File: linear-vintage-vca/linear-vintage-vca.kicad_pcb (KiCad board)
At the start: 2 copper layers, 50.5 x 110 mm, 57 parts, among them J1 Conn_02x08_Odd_Even, J10 Conn_01x02_Pin, J11 Conn_01x02_Pin, J2 AudioJack2, J3 AudioJack2, J4 AudioJack2, J5 AudioJack2, J6 AudioJack2, J7 AudioJack2, J8 AudioJack2, J9 AudioJack2, Q1 BC556, Q2 BC556, SW1 SW_SPDT_321, SW2 SW_SPDT_321, U1 LM13700, U2 TL072, U3 TL072

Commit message: Version sent to jlcpcb
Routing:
- net Net-(J11-Pin_2): track 50.0 -> 53.9 mm
- net Net-(J11-Pin_1): track 18.1 -> 19.2 mm
- net Net-(R4-Pad2): track 40.9 -> 41.8 mm
- net Net-(SW2-C): track 19.2 -> 20.0 mm
- net Net-(U3A--): track 58.8 -> 59.6 mm
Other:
- board text added: "2025"
- board text added: "Linear VCA"
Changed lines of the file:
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@@
 			(outputformat 1)
 			(mirror no)
-			(drillshape 1)
+			(drillshape 0)
 			(scaleselection 1)
-			(outputdirectory "")
+			(outputdirectory "gerber")
 		)
 	)
@@
 		(tags "Resistor Axial_DIN0207 series Axial Horizontal pin pitch 7.62mm 0.25W = 1/4W length 6.3mm diameter 2.5mm")
 		(property "Reference" "R21"
-			(at -2.38 0.2 90)
+			(at 10.42 0 180)
 			(layer "F.SilkS")
 			(effects
@@
 		(tags "Resistor Axial_DIN0207 series Axial Horizontal pin pitch 7.62mm 0.25W = 1/4W length 6.3mm diameter 2.5mm")
 		(property "Reference" "R22"
-			(at 10.01 0 90)
+			(at -2.79 -0.8 180)
 			(layer "F.SilkS")
 			(effects
@@
 		(tags "C Rect series Radial pin pitch 5.00mm length 7mm width 2mm Capacitor")
 		(property "Reference" "C5"
-			(at 7.533333 0 0)
+			(at 5.133333 2 0)
 			(layer "F.SilkS")
 			(effects
@@
 		(tags "TRS audio jack stereo horizontal")
 		(property "Reference" "J8"
-			(at 0 -6 90)
+			(at 5.605 5 180)
 			(layer "F.SilkS")
 			(effects
@@
 	)
 	(gr_text "Output"
-		(at 100.4 165.4 90)
+		(at 100.2 165.4 90)
 		(layer "F.SilkS")
 		(effects
@@
 		)
 	)
+	(gr_text "Linear VCA"
+		(at 96 118.8 0)
+		(layer "B.SilkS")
+		(effects
+			(font
+				(size 5 5)
+				(thickness 0.7)
+			)
+			(justify left bottom mirror)
+		)
+	)
+	(gr_text "2025"
+		(at 72 123.4 0)
+		(layer "B.SilkS")
+		(effects
+			(font
+				(size 3 3)
+				(thickness 0.3)
+			)
+			(justify left bottom mirror)
+		)
+	)
 	(dimension
 		(type orthogonal)
@@
 	)
 	(segment
-		(start 77.2 154.533333)
-		(end 77.2 143.061667)
+		(start 78.666667 156)
+		(end 76.2 153.533333)
 		(width 0.4)
 		(layer "B.Cu")
@@
 	)
 	(segment
-		(start 77.2 143.061667)
-		(end 81.166667 139.095)
+		(start 76.2 153.533333)
+		(end 76.2 144.061667)
 		(width 0.4)
 		(layer "B.Cu")
@@
 	)
 	(segment
-		(start 78.666667 156)
-		(end 77.2 154.533333)
+		(start 76.2 144.061667)
+		(end 81.166667 139.095)
 		(width 0.4)
 		(layer "B.Cu")
@@
 	)
 	(segment
-		(start 74.512083 134.487917)
-		(end 74.6 134.4)
+		(start 75.6 165)
+		(end 75.6 135.4)
 		(width 0.4)
 		(layer "B.Cu")
@@
 	)
 	(segment
-		(start 73.143333 134.487917)
-		(end 74.512083 134.487917)
+		(start 73.143333 167.2)
+		(end 73.143333 167.343333)
 		(width 0.4)
 		(layer "B.Cu")
@@
 	)
 	(segment
-		(start 73.2 167.4)
-		(end 74.6 166)
+		(start 74.512083 134.487917)
+		(end 74.6 134.4)
 		(width 0.4)
 		(layer "B.Cu")
@@
 	)
 	(segment
-		(start 73.186967 129.386967)
-		(end 73.143333 129.386967)
+		(start 73.143333 134.487917)
+		(end 74.512083 134.487917)
 		(width 0.4)
 		(layer "B.Cu")
@@
 	)
 	(segment
-		(start 74.6 130.8)
-		(end 73.186967 129.386967)
+		(start 75.6 135.4)
+		(end 74.6 134.4)
 		(width 0.4)
 		(layer "B.Cu")
@@
 	)
 	(segment
-		(start 73.143333 167.2)
-		(end 73.143333 167.343333)
+		(start 73.186967 129.386967)
+		(end 73.143333 129.386967)
 		(width 0.4)
 		(layer "B.Cu")
@@
 	)
 	(segment
-		(start 74.6 134.4)
-		(end 74.6 130.8)
+		(start 74.6 130.8)
+		(end 73.186967 129.386967)
 		(width 0.4)
 		(layer "B.Cu")
@@
 	)
 	(segment
-		(start 74.6 166)
-		(end 74.6 134.4)
+		(start 73.2 167.4)
+		(end 75.6 165)
+		(width 0.4)
+		(layer "B.Cu")
+		(net 32)
+	)
+	(segment
+		(start 74.6 134.4)
+		(end 74.6 130.8)
 		(width 0.4)
 		(layer "B.Cu")
@@
 	)
 	(segment
-		(start 87 130.023333)
+		(start 86.6 129.623333)
 		(end 84.976667 128)
 		(width 0.4)
@@
 	)
 	(segment
-		(start 89.2 151.6)
-		(end 87 149.4)
+		(start 89.19 151.61)
+		(end 89.2 151.6)
 		(width 0.4)
 		(layer "B.Cu")
@@
 	)
 	(segment
-		(start 89.19 151.61)
-		(end 89.2 151.6)
+		(start 86.6 149)
+		(end 86.6 129.623333)
 		(width 0.4)
 		(layer "B.Cu")
@@
 	)
 	(segment
-		(start 87 149.4)
-		(end 87 130.023333)
+		(start 89.2 151.6)
+		(end 86.6 149)
 		(width 0.4)
 		(layer "B.Cu")
@@
 	)
 	(segment
-		(start 96.678578 146.91347)
-		(end 96.82 146.91347)
+		(start 75.4 107.260533)
+		(end 73.143333 105.003866)
 		(width 0.4)
 		(layer "B.Cu")
@@
 	)
 	(segment
-		(start 75.4 107.260533)
-		(end 73.143333 105.003866)
+		(start 75.4 117.8)
+		(end 75.4 107.260533)
 		(width 0.4)
 		(layer "B.Cu")
@@
 	)
 	(segment
-		(start 75.4 117.8)
-		(end 75.4 107.260533)
+		(start 86.46 125.46)
+		(end 93 132)
 		(width 0.4)
 		(layer "B.Cu")
@@
 	)
 	(segment
-		(start 96.82 146.91347)
+		(start 96.82 147.62)
 		(end 96.82 151.6)
 		(width 0.4)
@@
 	(segment
 		(start 84.976667 125.46)
-		(end 87.601 128.084333)
+		(end 86.46 125.46)
 		(width 0.4)
 		(layer "B.Cu")
@@
 	)
 	(segment
-		(start 87.601 128.084333)
-		(end 87.601 137.835892)
+		(start 93 132)
+		(end 93 143.8)
 		(width 0.4)
 		(layer "B.Cu")
@@
 	)
 	(segment
-		(start 87.601 137.835892)
-		(end 96.678578 146.91347)
+		(start 93 143.8)
+		(end 96.82 147.62)
 		(width 0.4)
 		(layer "B.Cu")
@@
 	)
 	(segment
-		(start 83.666667 153.835)
-		(end 82.431667 152.6)
+		(start 84.4 155.266667)
+		(end 84.4 152.6)
 		(width 0.4)
 		(layer "B.Cu")
@@
 	)
 	(segment
-		(start 82.6 119)
-		(end 85.2 116.4)
+		(start 82.431667 152.6)
+		(end 84.4 152.6)
 		(width 0.4)
 		(layer "B.Cu")
@@
 	)
 	(segment
-		(start 85.2 109.823333)
-		(end 84.976667 109.6)
+		(start 84.4 137)
+		(end 82.6 135.2)
 		(width 0.4)
 		(layer "B.Cu")
@@
 	)
 	(segment
-		(start 85.2 116.4)
-		(end 85.2 109.823333)
+		(start 84.4 148.4)
+		(end 84.4 137)
 		(width 0.4)
 		(layer "B.Cu")
@@
 	)
 	(segment
-		(start 82.6 137.214932)
-		(end 82.6 119)
+		(start 85.2 109.823333)
+		(end 84.976667 109.6)
 		(width 0.4)
 		(layer "B.Cu")
@@
 	)
 	(segment
-		(start 83.6 138.214932)
-		(end 82.6 137.214932)
+		(start 82.6 119)
+		(end 85.2 116.4)
 		(width 0.4)
 		(layer "B.Cu")
@@
 	)
 	(segment
-		(start 81.166667 148.495)
-		(end 83.6 146.061667)
+		(start 82.6 135.2)
+		(end 82.6 119)
 		(width 0.4)
 		(layer "B.Cu")
@@
 	)
 	(segment
-		(start 82.431667 149.831667)
-		(end 82.431667 152.6)
+		(start 84.305 148.495)
+		(end 84.4 148.4)
 		(width 0.4)
 		(layer "B.Cu")
@@
 	)
 	(segment
-		(start 83.666667 156)
-		(end 83.666667 153.835)
+		(start 85.2 116.4)
+		(end 85.2 109.823333)
+		(width 0.4)
+		(layer "B.Cu")
+		(net 44)
+	)
+	(segment
+		(start 81.166667 148.495)
+		(end 84.305 148.495)
 		(width 0.4)
 		(layer "B.Cu")
@@
 	)
 	(segment
-		(start 83.6 146.061667)
-		(end 83.6 138.214932)
+		(start 83.666667 156)
+		(end 84.4 155.266667)
 		(width 0.4)
 		(layer "B.Cu")
@@
 	)
 	(segment
-		(start 81.166667 148.566667)
-		(end 82.431667 149.831667)
+		(start 84.4 152.6)
+		(end 84.4 148.4)
 		(width 0.4)
 		(layer "B.Cu")
@@
 	)
 	(segment
+		(start 77.6 150.308333)
+		(end 77.6 146.2)
+		(width 0.4)
+		(layer "F.Cu")
+		(net 46)
+	)
+	(segment
 		(start 88.5 143.795)
 		(end 81.166667 143.795)
@@
 	)
 	(segment
-		(start 79.891667 152.6)
-		(end 78.2 150.908333)
+		(start 77.6 146.2)
+		(end 80.005 143.795)
 		(width 0.4)
-		(layer "B.Cu")
+		(layer "F.Cu")
 		(net 46)
 	)
 	(segment
-		(start 78.2 146.761667)
+		(start 80.005 143.795)
 		(end 81.166667 143.795)
 		(width 0.4)
-		(layer "B.Cu")
+		(layer "F.Cu")
 		(net 46)
 	)
 	(segment
-		(start 78.2 150.908333)
-		(end 78.2 146.761667)
+		(start 79.891667 152.6)
+		(end 77.6 150.308333)
 		(width 0.4)
-		(layer "B.Cu")
+		(layer "F.Cu")
 		(net 46)
 	)

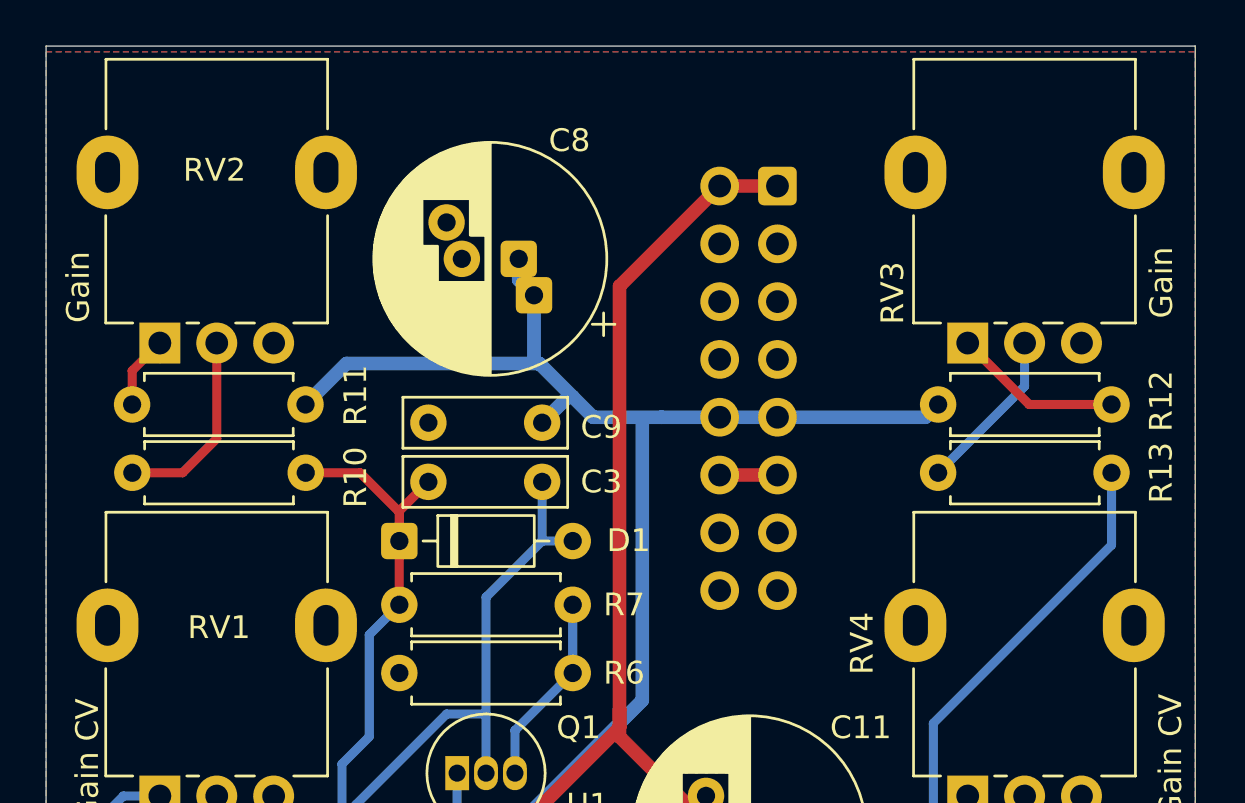
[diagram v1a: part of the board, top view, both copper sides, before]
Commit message: Fix potentiometers footprint.
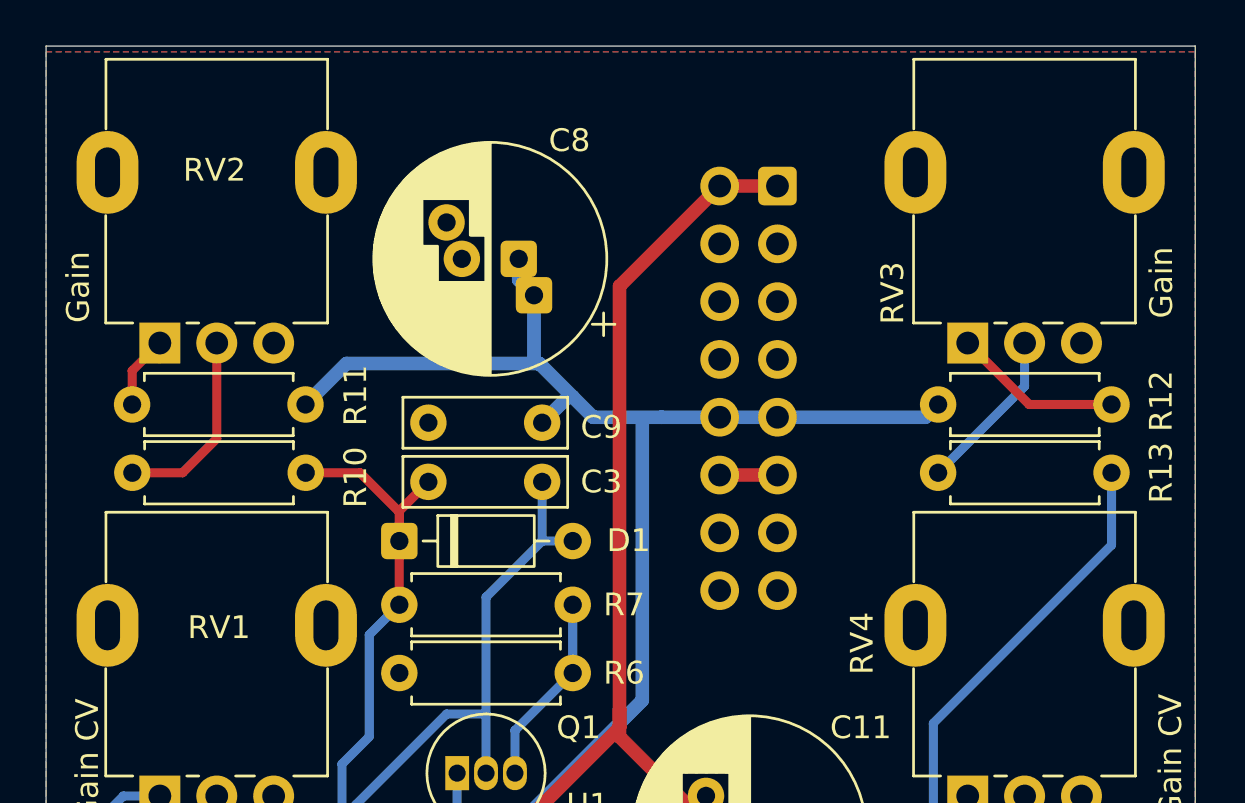
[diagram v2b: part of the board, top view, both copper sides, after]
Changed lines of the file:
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@@
 		(pad "" thru_hole oval
 			(at -4.8 0 180)
-			(size 2.72 3.24)
-			(drill oval 1.1 1.8)
+			(size 2.72 3.64)
+			(drill oval 1.1 2.2)
 			(layers "*.Cu" "*.Mask")
 			(remove_unused_layers no)
@@
 		(pad "" thru_hole oval
 			(at 4.8 0 180)
-			(size 2.72 3.24)
-			(drill oval 1.1 1.8)
+			(size 2.72 3.64)
+			(drill oval 1.1 2.2)
 			(layers "*.Cu" "*.Mask")
 			(remove_unused_layers no)
@@
 		(pad "" thru_hole oval
 			(at -4.8 0 180)
-			(size 2.72 3.24)
-			(drill oval 1.1 1.8)
+			(size 2.72 3.64)
+			(drill oval 1.1 2.2)
 			(layers "*.Cu" "*.Mask")
 			(remove_unused_layers no)
@@
 		(pad "" thru_hole oval
 			(at 4.8 0 180)
-			(size 2.72 3.24)
-			(drill oval 1.1 1.8)
+			(size 2.72 3.64)
+			(drill oval 1.1 2.2)
 			(layers "*.Cu" "*.Mask")
 			(remove_unused_layers no)
@@
 		(pad "" thru_hole oval
 			(at -4.8 0 180)
-			(size 2.72 3.24)
-			(drill oval 1.1 1.8)
+			(size 2.72 3.64)
+			(drill oval 1.1 2.2)
 			(layers "*.Cu" "*.Mask")
 			(remove_unused_layers no)
@@
 		(pad "" thru_hole oval
 			(at 4.8 0 180)
-			(size 2.72 3.24)
-			(drill oval 1.1 1.8)
+			(size 2.72 3.64)
+			(drill oval 1.1 2.2)
 			(layers "*.Cu" "*.Mask")
 			(remove_unused_layers no)
@@
 		(pad "" thru_hole oval
 			(at -4.8 0 180)
-			(size 2.72 3.24)
-			(drill oval 1.1 1.8)
+			(size 2.72 3.64)
+			(drill oval 1.1 2.2)
 			(layers "*.Cu" "*.Mask")
 			(remove_unused_layers no)
@@
 		(pad "" thru_hole oval
 			(at 4.8 0 180)
-			(size 2.72 3.24)
-			(drill oval 1.1 1.8)
+			(size 2.72 3.64)
+			(drill oval 1.1 2.2)
 			(layers "*.Cu" "*.Mask")
 			(remove_unused_layers no)

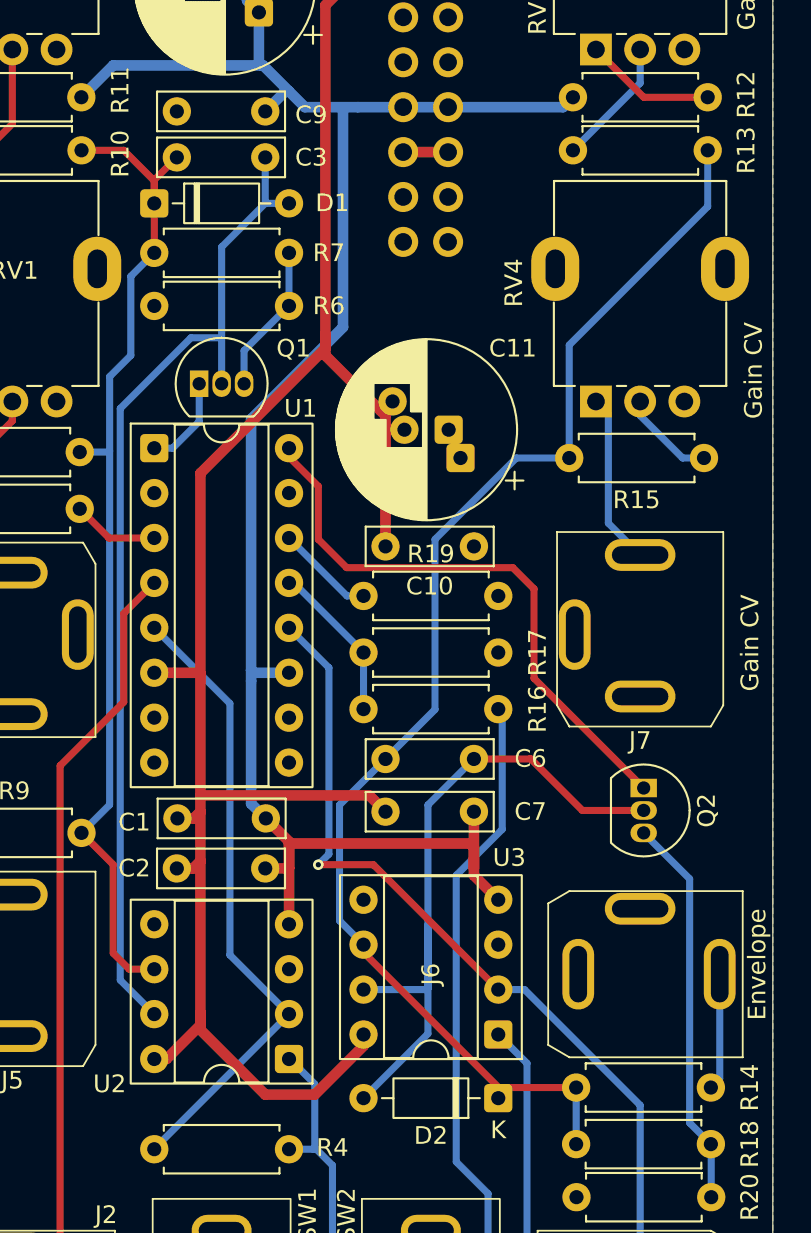
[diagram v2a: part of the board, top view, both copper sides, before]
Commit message: Cleaned up footprints
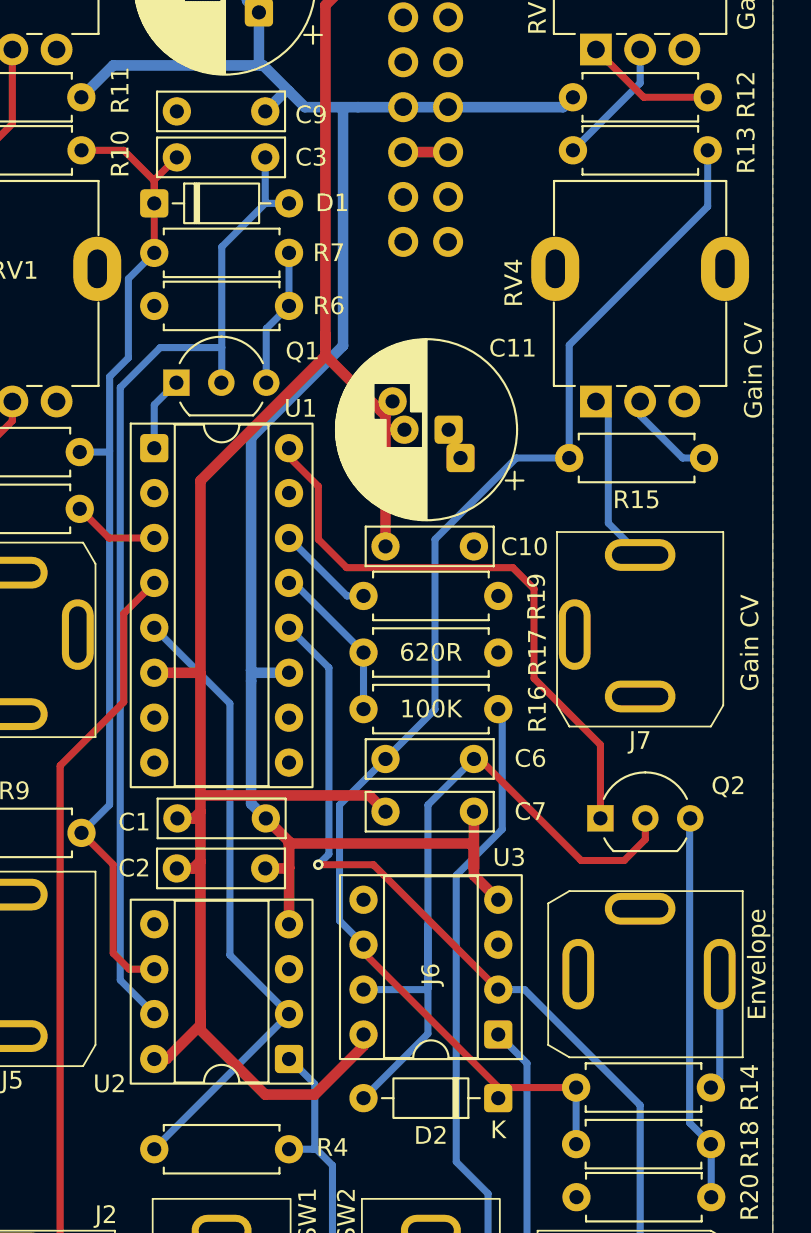
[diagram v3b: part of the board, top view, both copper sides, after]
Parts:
- Q1, Q2: footprint Package_TO_SOT_THT:TO-92_Inline -> Package_TO_SOT_THT:TO-92_Inline_Wide
- moved Q2 2.99 mm to (90.8, 115.8), turned to 0 degrees
- moved Q1 1.29 mm to (66.8, 91.1)
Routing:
- net Net-(D2-A): track 39.8 -> 42.8 mm
- net Net-(Q1-C): track 5.30 -> 4.22 mm
- net Net-(Q2-C): track 33.0 -> 33.7 mm
- net Net-(Q1-E): track 8.46 -> 7.89 mm
